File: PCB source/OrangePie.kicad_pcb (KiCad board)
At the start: 4 copper layers, 100 x 100 mm, 136 parts, among them J1 09031967921, J2 Orange pi 5 pro, J3 JST XH, J5 USB_C_Receptacle_USB2.0_16P, M1 Fan, Q1 AO3400A, Q2 AO3400A, Q4 AO3400A, Q5 MMBT3904, U1 PESD5V0S2BT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

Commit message: Prepare for boardhouse
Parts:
- added REF**: Part_Num_JLCPCB, PCM_JLCPCB:Part_Num_JLCPCB, F.Cu at (73.0, 68.3)
- added REF**: OSHW-Symbol_6.7x6mm_SilkScreen, Symbol:OSHW-Symbol_6.7x6mm_SilkScreen, B.Cu at (47.0, 66.6)
- added REF**: My_github, Symbol:My_github, B.Cu at (60.2, 68.1)
- added kibuzzard-67B62451: G***, kibuzzard-67B62451, B.Cu at (118.0, 87.0)
- added kibuzzard-67B62470: G***, kibuzzard-67B62470, B.Cu at (113.7, 91.1)
- added kibuzzard-67B6248A: G***, kibuzzard-67B6248A, B.Cu at (116.0, 91.2)
- added kibuzzard-67B6249A: G***, kibuzzard-67B6249A, B.Cu at (118.4, 91.2)
- added kibuzzard-67B7B9BD: G***, kibuzzard-67B7B9BD, F.Cu at (110.8, 93.4)
- added kibuzzard-67B7B9C6: G***, kibuzzard-67B7B9C6, F.Cu at (110.7, 98.4)
- added kibuzzard-67B7BB29: G***, kibuzzard-67B7BB29, F.Cu at (61.0, 125.0)
- added kibuzzard-67B7BD37: G***, kibuzzard-67B7BD37, F.Cu at (108.2, 59.2)
- added kibuzzard-67B7BFDD: G***, kibuzzard-67B7BFDD, F.Cu at (96.8, 109.2)
- added kibuzzard-67B7C21F: G***, kibuzzard-67B7C21F, B.Cu at (115.6, 86.9)
- added kibuzzard-67B7C241: G***, kibuzzard-67B7C241, B.Cu at (120.4, 87.0)
- moved C18 2.00 mm to (113.2, 83.8)
- moved C19 2.00 mm to (115.2, 82.8)
- moved C20 2.00 mm to (117.2, 82.8)
- moved C21 2.00 mm to (120.0, 94.2)
- moved C22 2.00 mm to (111.2, 91.5)
- moved C23 2.00 mm to (122.0, 93.4)
- moved C24 2.00 mm to (122.0, 92.4)
- moved C25 2.00 mm to (123.2, 88.3)
- moved D1 2.00 mm to (112.0, 95.0)
- moved D3 2.00 mm to (112.0, 96.8)
- moved R10 2.00 mm to (114.8, 95.2)
- moved R11 2.00 mm to (114.8, 96.6)
- moved R9 2.00 mm to (123.2, 90.3)
- moved TP1 2.00 mm to (117.0, 88.0)
- moved TP2 2.00 mm to (119.4, 88.0)
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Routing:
- net /USB HUB/USB_CAN.D+: track 49.1 -> 51.1 mm
- net /USB HUB/USB_CAN.D-: track 49.1 -> 51.1 mm
- net /Can Transiver1/CAN_TR.RXD: track 44.7 -> 45.5 mm
- net /Can Transiver1/CAN_TR.TXD: track 43.7 -> 44.6 mm
- net /Can Transiver/CAN_TR.TXD: track 46.3 -> 45.7 mm
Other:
- board text added: "ASSEMBLY STICKER"
- board text added: "CAN2USB"
- board text added: "Card"
- board text added: "Crystal clear audio"
- board text added: "DESIGNED IN POLAND"
- board text added: "Device info:"
- board text added: "ESD SENSETIVE DEVICE"
- board text added: "MADE IN CHINA BY JLCPCB"
- board text added: "Modu"
- board text added: "Orange Pi 5 pro adapter for ModuCard System"
- board text added: "PCM2704"
- board text added: "PGOOD"
- board text added: "PROJECT Rev. ${REVISION}"
- board text added: "SBC FAN"
- board text added: "SPEAKER"
- board text added: "i"
- board text removed: "Dominik Pluta Artem Horiunov"
- board text removed: "PROJECT Rev. ${REVISION} TEMPLATE Rev. 1.0.0"
- board text removed: "Template authors:"

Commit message: Add 22R resistors to USB
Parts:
- added R34: 0Ω, PCM_JLCPCB:R_0402, F.Cu at (111.0, 125.8)
- added R35: 0Ω, PCM_JLCPCB:R_0402, F.Cu at (103.4, 125.7)
- added R42: 22Ω, PCM_JLCPCB:R_0402, F.Cu at (102.6, 58.8)
- added R43: 22Ω, PCM_JLCPCB:R_0402, F.Cu at (102.6, 57.8)
- added R44: 22Ω, PCM_JLCPCB:R_0402, F.Cu at (81.8, 62.4)
- added R45: 22Ω, PCM_JLCPCB:R_0402, F.Cu at (80.8, 62.4)
- R14, R15: value 10kΩ -> 22Ω
- moved R14 60.9 mm to (100.8, 65.8)
- moved R15 60.1 mm to (99.6, 65.8)
- moved R16 0.10 mm to (118.1, 72.2)
- moved R17 0.10 mm to (120.3, 72.2)
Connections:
- J2 pad 43: /DIN41612 connector/USB_DEBUG.D+ -> /OrangePi 5 pro Header/USB_SBCF.D+
- J2 pad 44: /DIN41612 connector/USB_DEBUG.D- -> /OrangePi 5 pro Header/USB_SBCF.D-
- R14 pad 1: Net-(U6-STB) -> /USB-CAN/USB_CANF.D-
- R14 pad 2: GND -> /USB HUB/USB_CAN.D-
- R15 pad 1: Net-(U7-STB) -> /USB-CAN/USB_CANF.D+
- R15 pad 2: GND -> /USB HUB/USB_CAN.D+
- R19 pad 2: /Audio Codec/USB_AUDIO.D+ -> /Audio Codec/USB_AUDIOF.D+
- U3 pad 33: /USB HUB/USB_CAN.D- -> /USB-CAN/USB_CANF.D-
- U3 pad 34: /USB HUB/USB_CAN.D+ -> /USB-CAN/USB_CANF.D+
- U9 pad 8: /Audio Codec/USB_AUDIO.D- -> /Audio Codec/USB_AUDIOF.D-
- U9 pad 9: /Audio Codec/USB_AUDIO.D+ -> /Audio Codec/USB_AUDIOF.D+
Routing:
- net /USB HUB/USB_CAN.D-: track 51.1 -> 3.42 mm
- net /USB HUB/USB_CAN.D+: track 51.1 -> 4.02 mm
- net /USB-CAN/USB_CANF.D-: track 0.00 -> 47.1 mm
- net /USB-CAN/USB_CANF.D+: track 0.00 -> 46.5 mm
- net /Audio Codec/USB_AUDIO.D-: track 30.3 -> 8.38 mm
- net /Audio Codec/USB_AUDIO.D+: track 30.3 -> 8.33 mm
- net /Audio Codec/USB_AUDIOF.D-: track 0.00 -> 21.8 mm
- net /Audio Codec/USB_AUDIOF.D+: track 0.00 -> 21.8 mm
- net /DIN41612 connector/USB_DEBUG.D-: track 114.1 -> 111.1 mm
- net /DIN41612 connector/USB_DEBUG.D+: track 113.8 -> 110.9 mm
- net /OrangePi 5 pro Header/USB_SBCF.D+: track 0.00 -> 2.22 mm
- net /OrangePi 5 pro Header/USB_SBCF.D-: track 0.00 -> 2.19 mm
- added copper zone on B.Cu, net /5v buck/V_{IN}
- added copper zone on B.Cu, net GND

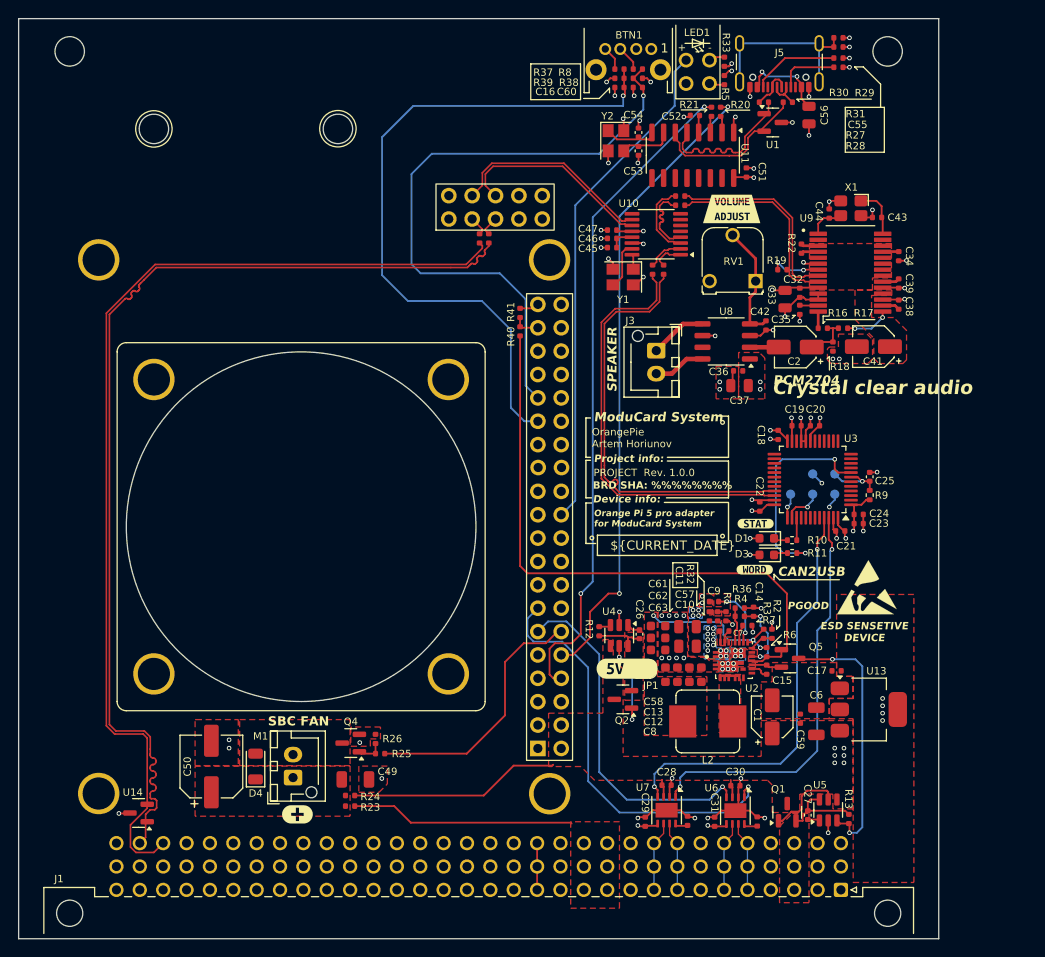
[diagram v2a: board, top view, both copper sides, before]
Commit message: Check BOM and add tooling holes
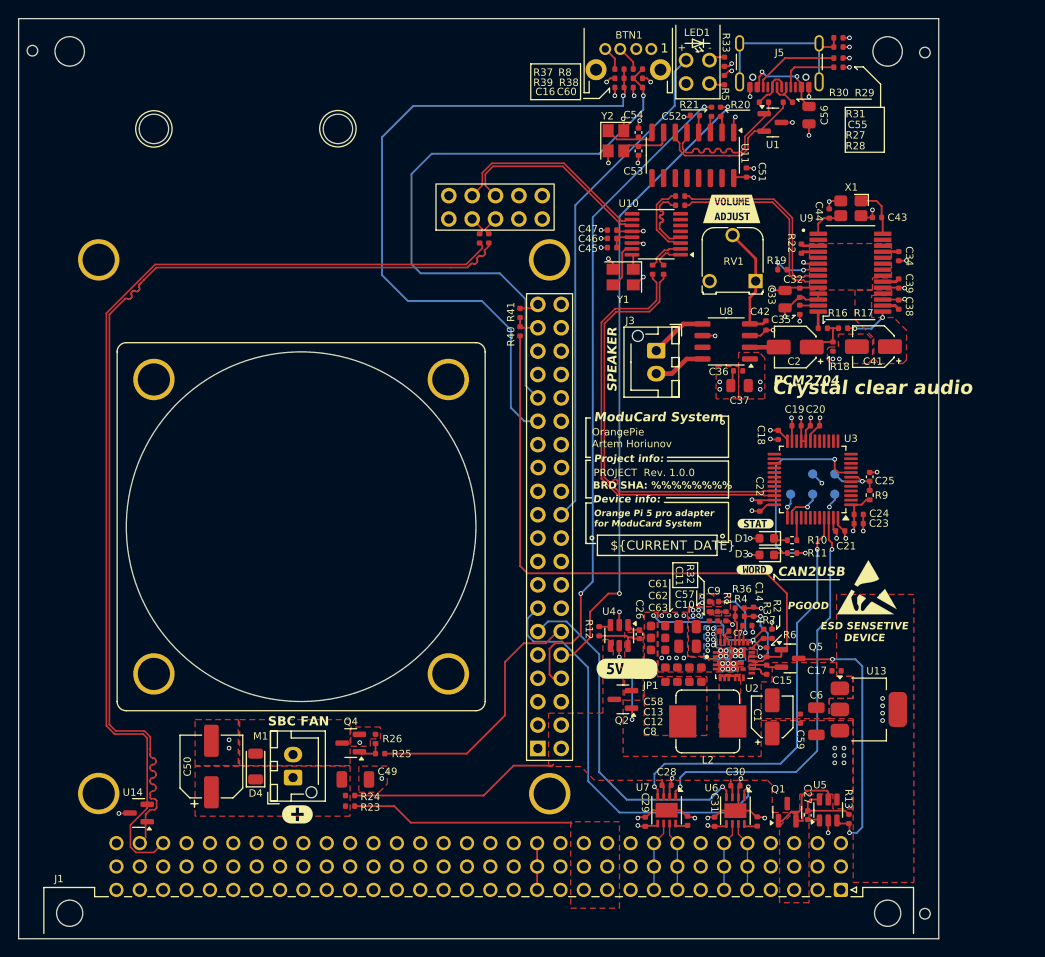
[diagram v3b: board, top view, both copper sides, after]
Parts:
- added REF**: Hole_Tooling_JLCPCB, PCM_JLCPCB:Hole_Tooling_JLCPCB, F.Cu at (129.2, 42.2)
- added REF**: Hole_Tooling_JLCPCB, PCM_JLCPCB:Hole_Tooling_JLCPCB, F.Cu at (129.2, 135.8)
- added REF**: Hole_Tooling_JLCPCB, PCM_JLCPCB:Hole_Tooling_JLCPCB, F.Cu at (32.2, 42.0)
